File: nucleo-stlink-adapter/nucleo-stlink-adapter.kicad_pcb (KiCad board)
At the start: 2 copper layers, 29 x 17.5 mm, 4 parts, among them J1 Conn_02x05_Odd_Even, J2 Conn_01x06_Female, SW1 RESET

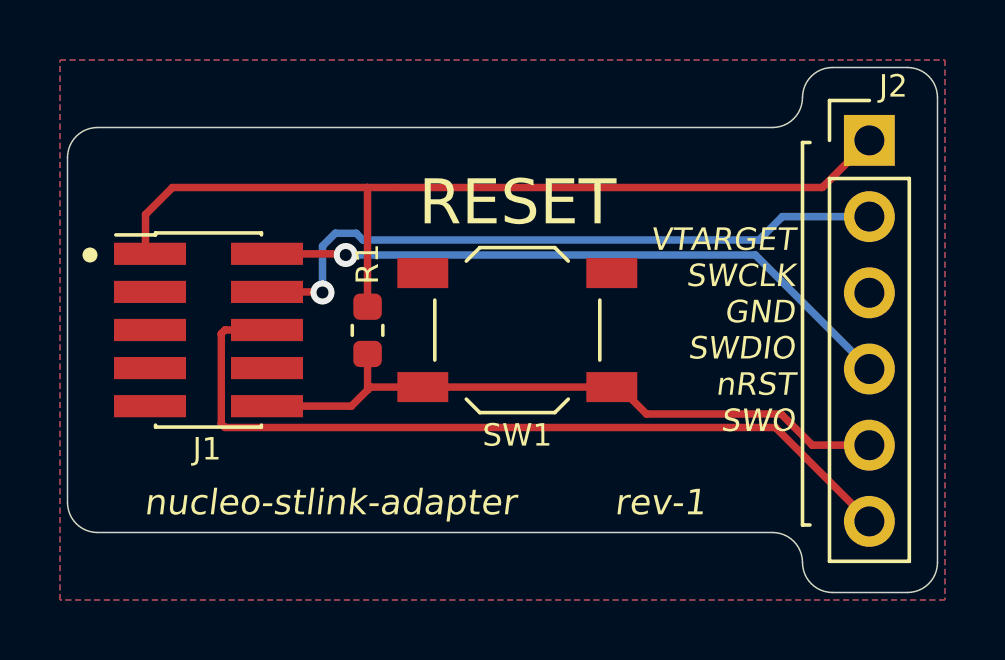
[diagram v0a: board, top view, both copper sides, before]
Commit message: Cleaned up schematic and board
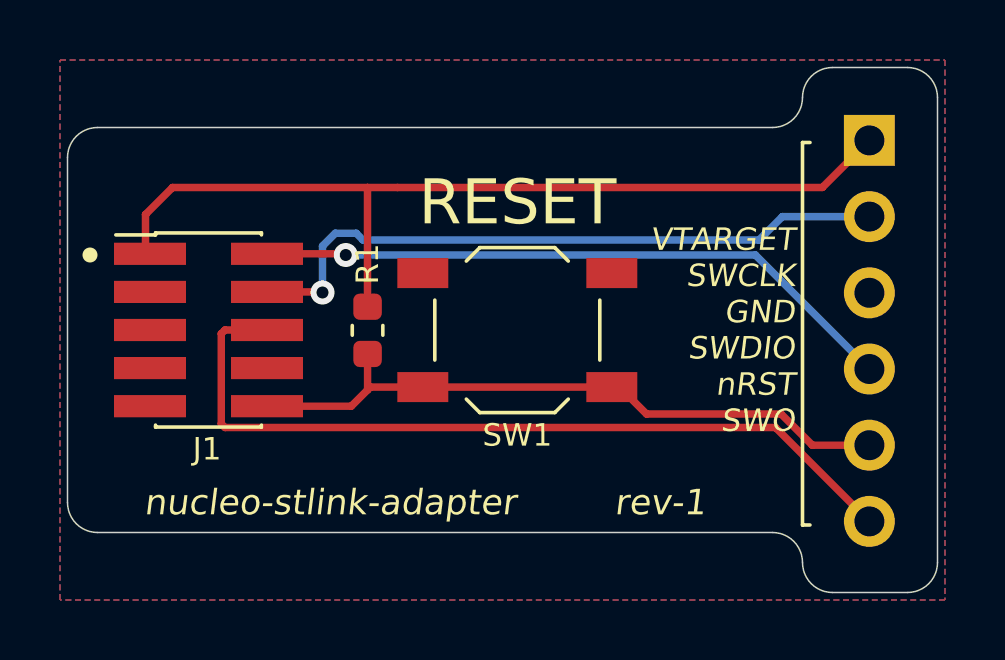
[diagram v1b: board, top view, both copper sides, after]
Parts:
- J2: moved to B.Cu
- turned J2 to 180 degrees
